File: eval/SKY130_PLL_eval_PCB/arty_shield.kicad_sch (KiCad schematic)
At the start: 1 part

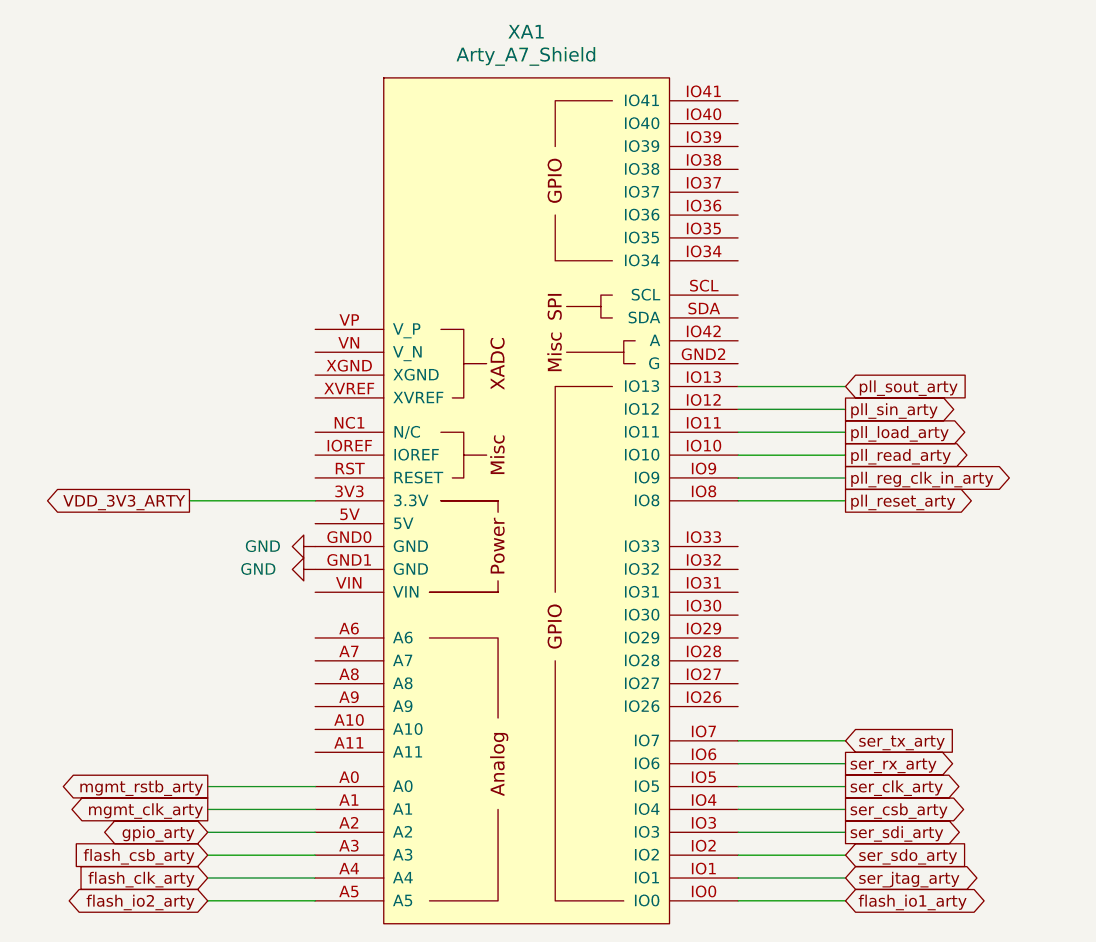
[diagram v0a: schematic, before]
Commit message: eval pcb added
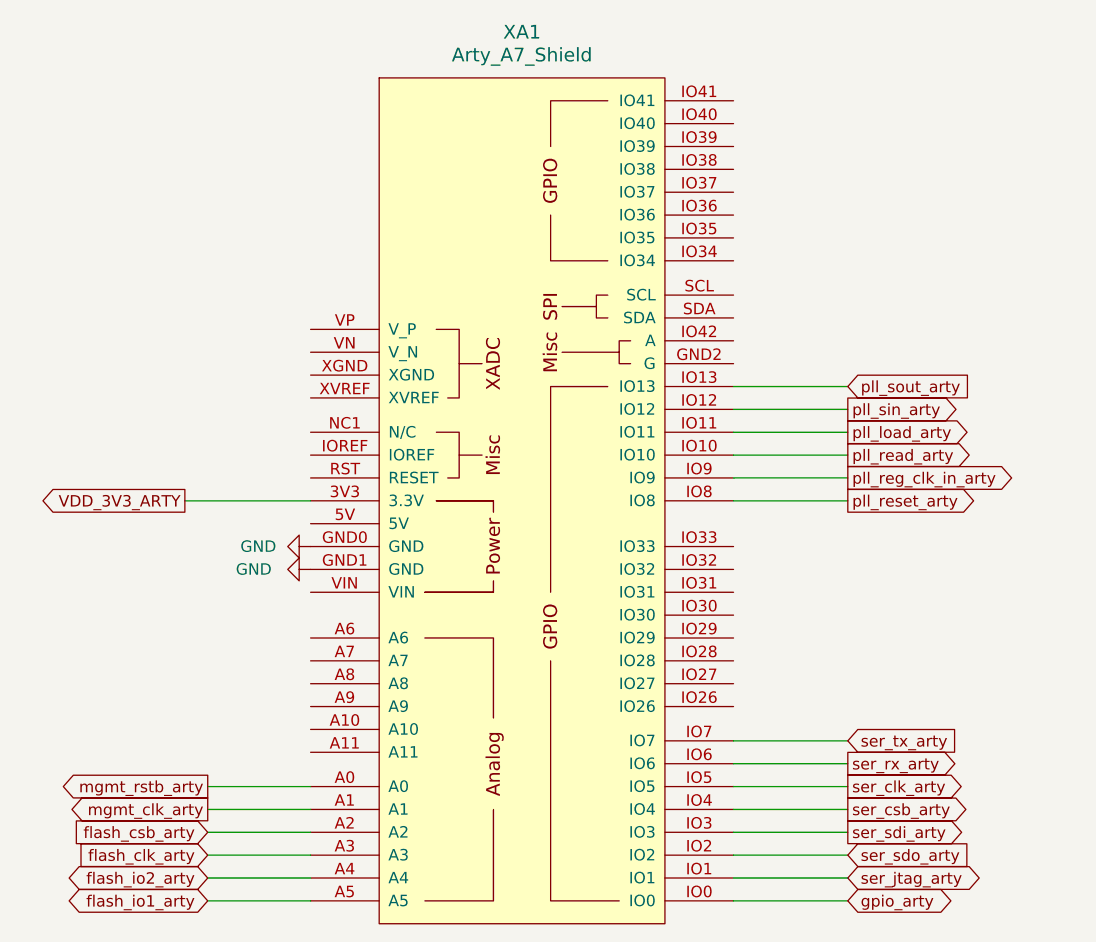
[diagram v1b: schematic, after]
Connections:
- net flash_clk_arty: now also XA1.A3; no longer XA1.A4
- net flash_csb_arty: now also XA1.A2; no longer XA1.A3
- net flash_io1_arty: now also XA1.A5; no longer XA1.IO0
- net flash_io2_arty: now also XA1.A4; no longer XA1.A5
- net gpio_arty: now also XA1.IO0; no longer XA1.A2
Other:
- moved on the sheet: XA1
